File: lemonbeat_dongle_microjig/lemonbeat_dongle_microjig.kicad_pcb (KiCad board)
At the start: 4 copper layers, 50 x 42 mm, 21 parts, among them J1 Prog, J2 Main, J202 Prog, J3 Si4467

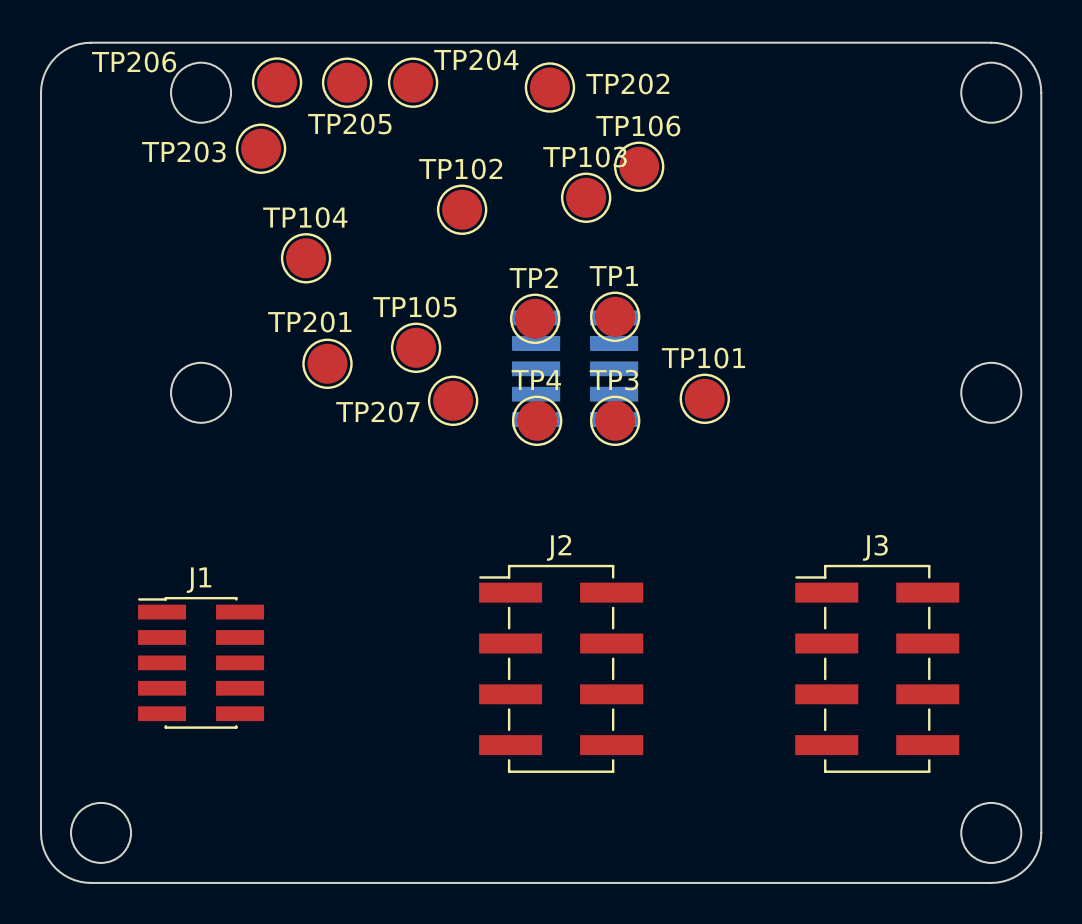
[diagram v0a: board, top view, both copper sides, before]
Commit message: dongle: microjig: routing, silk screen & LCSC part numbers
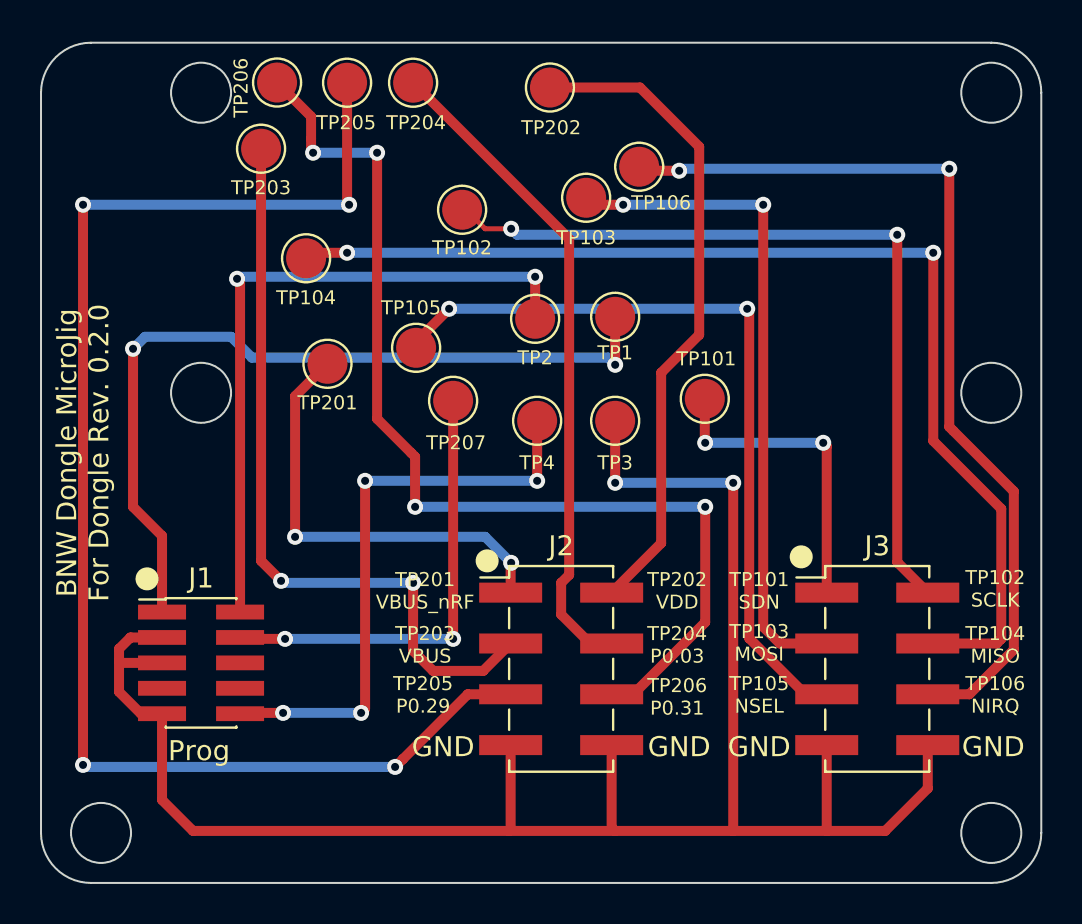
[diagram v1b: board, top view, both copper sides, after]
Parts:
- removed J202: Prog, Connector_PinHeader_1.27mm:PinHeader_2x05_P1.27mm_Vertical_SMD
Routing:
- net GND: track 0.00 -> 95.0 mm, vias 0 -> 2
- net Net-(J2-Pad5): track 0.00 -> 70.4 mm, vias 0 -> 4
- net Net-(J3-Pad4): track 0.00 -> 55.9 mm, vias 0 -> 2
- net Net-(J2-Pad6): track 0.00 -> 52.4 mm, vias 0 -> 4
- net Net-(J3-Pad6): track 0.00 -> 46.2 mm, vias 0 -> 2
- net VDD: track 0.00 -> 41.1 mm, vias 0 -> 2
- net Net-(J3-Pad2): track 0.00 -> 40.5 mm, vias 0 -> 2
- net Net-(J3-Pad5): track 0.00 -> 39.1 mm, vias 0 -> 2
- net Net-(J2-Pad3): track 0.00 -> 37.9 mm, vias 0 -> 2
- net /SWDIO: track 0.00 -> 33.8 mm, vias 0 -> 2
- net Net-(J3-Pad3): track 0.00 -> 33.6 mm, vias 0 -> 2
- net Net-(J2-Pad4): track 0.00 -> 33.1 mm
- net Net-(J2-Pad2): track 0.00 -> 32.8 mm
- net /RESET: track 0.00 -> 29.3 mm, vias 0 -> 4
- net /SWDCLK: track 0.00 -> 22.6 mm, vias 0 -> 2
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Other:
- copper layers 4 -> 2
- board text added: "BNW Dongle MicroJig For Dongle Rev. 0.2.0"
- board text added: "GND"
- board text added: "Prog"
- board text added: "TP101 SDN"
- board text added: "TP102 SCLK"
- board text added: "TP103 MOSI"
- board text added: "TP104 MISO"
- board text added: "TP105 NSEL"
- board text added: "TP106 NIRQ"
- board text added: "TP201 VBUS_nRF"
- board text added: "TP202 VDD"
- board text added: "TP203 VBUS"
- board text added: "TP204 P0.03"
- board text added: "TP205 P0.29"
- board text added: "TP206 P0.31"
